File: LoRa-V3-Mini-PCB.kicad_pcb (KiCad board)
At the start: 2 copper layers, 52 x 18 mm, 24 parts, among them Q1 SI2367DS-T1-GE3, SW1 434331045822, SW2 434331045816, U1 114993121, U2 BR24G1MFVT, U3 SHT40, U4 TSL25911

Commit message: move global components into project library
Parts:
- C1, C10, C11, C2, C3, C5: footprint 1GlobalFootprintsLibrary:C_0603_nominal -> 1projectLibrary:C_0603_nominal
- R1, R2, R3, R4: footprint 1GlobalFootprintsLibrary:R_0603_nominal -> 1projectLibrary:R_0603_nominal

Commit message: update 3d models / footprints
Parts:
- U1: footprint 1GlobalFootprintsLibrary:LoRa-E5 -> 1projectLibrary:LoRa-E5
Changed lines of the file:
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@@
 		)
 	)
-	(footprint "1GlobalFootprintsLibrary:LoRa-E5"
+	(footprint "1projectLibrary:LoRa-E5"
 		(layer "F.Cu")
 		(at 150.91 103.5)
@@
 			)
 		)
-		(property "Footprint" "1GlobalFootprintsLibrary:LoRa-E5"
+		(property "Footprint" "1projectLibrary:LoRa-E5"
 			(at 0 13 0)
 			(unlocked yes)
@@
 			(pintype "input+no_connect")
 		)
-		(model "C:/Users/pasca/Documents/Projects/Electronica/myComponents/1global3dmodels/LoRa-E5-HF_3D_File.stp"
+		(model "${KIPRJMOD}/inputs/3dmodels/LoRa-E5-HF_3D_File.stp"
 			(offset
 				(xyz 0 0 2.6)
@@
 	)
 	(zone
-		(net 15)
-		(net_name "SWDIO")
-		(layer "F.Cu")
-		(name "$teardrop_padvia$")
-		(hatch full 0.1)
-		(priority 30010)
-		(attr
-			(teardrop
-				(type padvia)
-			)
-		)
-		(connect_pads yes
-			(clearance 0)
-		)
-		(min_thickness 0.0254)
-		(filled_areas_thickness no)
-		(fill yes
-			(thermal_gap 0.5)
-			(thermal_bridge_width 0.5)
-			(island_removal_mode 1)
-			(island_area_min 10)
-		)
-		(polygon
-			(pts
-				(xy 145.96 102.125) (xy 145.96 102.375) (xy 146.526061 102.573358) (xy 146.661 102.25) (xy 146.526061 101.926642)
-			)
-		)
-	)
-	(zone
 		(net 7)
 		(net_name "I2C2-SDA")
@@
 	)
 	(zone
-		(net 5)
-		(net_name "~{Enable-3.3V-Switched}")
-		(layer "F.Cu")
-		(name "$teardrop_padvia$")
-		(hatch full 0.1)
-		(priority 30012)
-		(attr
-			(teardrop
-				(type padvia)
-			)
-		)
-		(connect_pads yes
-			(clearance 0)
-		)
-		(min_thickness 0.0254)
-		(filled_areas_thickness no)
-		(fill yes
-			(thermal_gap 0.5)
-			(thermal_bridge_width 0.5)
-			(island_removal_mode 1)
-			(island_area_min 10)
-		)
-		(polygon
-			(pts
-				(xy 152.035 108.45) (xy 152.285 108.45) (xy 152.483358 107.883939) (xy 152.16 107.749) (xy 151.836642 107.883939)
-			)
-		)
-	)
-	(zone
 		(net 4)
 		(net_name "+BATT")
@@
 			)
 		)
-	)
-	(zone
-		(net 10)
-		(net_name "Net-(U1-RST)")
-		(layer "F.Cu")
-		(name "$teardrop_padvia$")
-		(hatch full 0.1)
-		(priority 30009)
-		(attr
-			(teardrop
-				(type padvia)
-			)
-		)
-		(connect_pads yes
-			(clearance 0)
-		)
-		(min_thickness 0.0254)
-		(filled_areas_thickness no)
-		(fill yes
-			(thermal_gap 0.5)
-			(thermal_bridge_width 0.5)
-			(island_removal_mode 1)
-			(island_area_min 10)
-		)
-		(polygon
-			(pts
-				(xy 155.86 104.875) (xy 155.86 104.625) (xy 155.293939 104.426642) (xy 155.159 104.75) (xy 155.293939 105.073358)
-			)
-		)

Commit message: using project lib io global
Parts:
- U3: footprint 1GlobalFootprintsLibrary:SHT4X -> 1projectLibrary:SHT4X
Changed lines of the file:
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@@
 		)
 	)
-	(footprint "1GlobalFootprintsLibrary:SHT4X"
+	(footprint "1projectLibrary:SHT4X"
 		(layer "F.Cu")
 		(at 130.41 108.5 180)
@@
 			)
 		)
-		(property "Footprint" "1GlobalFootprintsLibrary:SHT4X"
+		(property "Footprint" "1projectLibrary:SHT4X"
 			(at 0 4 180)
 			(unlocked yes)
@@
 			)
 		)
-		(property "Description" "SHT40"
+		(property "Description" "Digital Relative Humidity Temperature Sensor"
 			(at 0 0 180)
 			(unlocked yes)
@@
 			(pintype "power_in")
 		)
-		(model "C:/Users/pasca/Documents/Projects/Electronica/myComponents/1global3dmodels/SHT40-AD1B-R2.step"
+		(model "${KIPRJMOD}/inputs/3dmodels/SHT40-AD1B-R2.step"
 			(offset
 				(xyz 0 0 0)
@@
 		(attr through_hole)
 		(fp_rect
-			(start 32.004 -8.128)
-			(end -2.54 8.128)
+			(start -2.54 8.128)
+			(end 32.004 -8.128)
 			(stroke
 				(width 0.05)
@@
 			(layer "User.2")
 			(pts
-				(xy 164.914 95.372) (xy 130.37 95.372)
+				(xy 164.914 111.628) (xy 164.914 95.372)
 			)
-			(height 4.572)
-			(gr_text "34,5440 mm"
-				(at 147.642 89.65 0)
+			(height 4.318)
+			(gr_text "16,2560 mm"
+				(at 168.082 103.5 90)
 				(layer "User.2")
 				(effects
@@
 			(layer "User.2")
 			(pts
-				(xy 132.91 103.5) (xy 132.91 110.5866)
+				(xy 132.91 103.5) (xy 162.374 103.5)
 			)
-			(height 4.572)
-			(gr_text "7,0866 mm"
-				(at 127.188 107.0433 90)
+			(height -5.08)
+			(gr_text "29,4640 mm"
+				(at 147.642 97.27 0)
 				(layer "User.2")
 				(effects
@@
 			(layer "User.2")
 			(pts
-				(xy 132.91 103.5) (xy 162.374 103.5)
+				(xy 164.914 95.372) (xy 130.37 95.372)
 			)
-			(height -5.08)
-			(gr_text "29,4640 mm"
-				(at 147.642 97.27 0)
+			(height 4.572)
+			(gr_text "34,5440 mm"
+				(at 147.642 89.65 0)
 				(layer "User.2")
 				(effects
@@
 			(layer "User.2")
 			(pts
-				(xy 164.914 111.628) (xy 164.914 95.372)
+				(xy 132.91 103.5) (xy 132.91 110.5866)
 			)
-			(height 4.318)
-			(gr_text "16,2560 mm"
-				(at 168.082 103.5 90)
+			(height 4.572)
+			(gr_text "7,0866 mm"
+				(at 127.188 107.0433 90)
 				(layer "User.2")
 				(effects
@@
 			(thermal_bridge_angle 0)
 		)
-		(model "C:/Users/pasca/Documents/Projects/Electronica/myComponents/1global3dmodels/Keystone-108.stp"
+		(model "${KIPRJMOD}/inputs/3dmodels/Keystone-108.stp"
 			(offset
 				(xyz 14.75 0 0.4)
@@
 			)
 		)
-	)
-	(zone
-		(net 7)
-		(net_name "I2C2-SDA")
-		(layer "F.Cu")
-		(name "$teardrop_padvia$")
-		(hatch full 0.1)
-		(priority 30007)
-		(attr
-			(teardrop
-				(type padvia)
-			)
-		)
-		(connect_pads yes
-			(clearance 0)
-		)
-		(min_thickness 0.0254)
-		(filled_areas_thickness no)
-		(fill yes
-			(thermal_gap 0.5)
-			(thermal_bridge_width 0.5)
-			(island_removal_mode 1)
-			(island_area_min 10)
-		)
-		(polygon
-			(pts
-				(xy 131.36 108.775) (xy 131.36 109.025) (xy 131.926061 109.223358) (xy 132.061 108.9) (xy 131.926061 108.576642)
-			)
-		)

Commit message: update libraries
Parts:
- ANT1: footprint 1GlobalFootprintsLibrary:XDCR_ANT-868-CHP-T -> 1projectLibrary:XDCR_ANT-868-CHP-T
- F1, F2, F3: footprint Fiducial:Fiducial_0.75mm_Mask1.5mm -> Fiducial:Fiducial_0.5mm_Mask1mm
- SW2: footprint 1GlobalFootprintsLibrary:4341330258X6 -> 1projectLibrary:4341330258X6
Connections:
- SW1 pad 2: SWO -> GND
- SW1 pad 3: GND -> SWO
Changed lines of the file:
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@@
 		)
 	)
-	(footprint "Fiducial:Fiducial_0.75mm_Mask1.5mm"
+	(footprint "Fiducial:Fiducial_0.5mm_Mask1mm"
 		(layer "F.Cu")
 		(at 179.41 111 90)
-		(descr "Circular Fiducial, 0.75mm bare copper, 1.5mm soldermask opening (Level B)")
+		(descr "Circular Fiducial, 0.5mm bare copper, 1mm soldermask opening (Level C)")
 		(tags "fiducial")
 		(property "Reference" "F2"
-			(at 0 -2 -90)
+			(at 0 -1.5 90)
 			(layer "F.SilkS")
 			(hide yes)
@@
 		)
 		(property "Value" "Fiducial"
-			(at 0 2 -90)
+			(at 0 1.5 90)
 			(layer "F.Fab")
 			(effects
@@
 			)
 		)
-		(property "Footprint" "Fiducial:Fiducial_0.75mm_Mask1.5mm"
+		(property "Footprint" "Fiducial:Fiducial_0.5mm_Mask1mm"
 			(at 0 0 90)
 			(unlocked yes)
@@
 		(fp_circle
 			(center 0 0)
-			(end 1 0)
+			(end 0.75 0)
 			(stroke
 				(width 0.05)
@@
 		(fp_circle
 			(center 0 0)
-			(end 0.75 0)
+			(end 0.5 0)
 			(stroke
 				(width 0.1)
@@
 		)
 		(fp_text user "${REFERENCE}"
-			(at 0 0 -90)
+			(at 0 0 90)
 			(layer "F.Fab")
 			(effects
 				(font
-					(size 0.3 0.3)
-					(thickness 0.05)
+					(size 0.2 0.2)
+					(thickness 0.04)
 				)
 			)
@@
 		(pad "" smd circle
 			(at 0 0 90)
-			(size 0.75 0.75)
+			(size 0.5 0.5)
 			(layers "F.Cu" "F.Mask")
-			(solder_mask_margin 0.375)
-			(clearance 0.375)
+			(solder_mask_margin 0.25)
+			(clearance 0.25)
 		)
 	)
-	(footprint "Fiducial:Fiducial_0.75mm_Mask1.5mm"
+	(footprint "Fiducial:Fiducial_0.5mm_Mask1mm"
 		(layer "F.Cu")
 		(at 179.41 96 90)
-		(descr "Circular Fiducial, 0.75mm bare copper, 1.5mm soldermask opening (Level B)")
+		(descr "Circular Fiducial, 0.5mm bare copper, 1mm soldermask opening (Level C)")
 		(tags "fiducial")
 		(property "Reference" "F3"
-			(at 0 -2 -90)
+			(at 0 -1.5 90)
 			(layer "F.SilkS")
 			(hide yes)
@@
 		)
 		(property "Value" "Fiducial"
-			(at 0 2 -90)
+			(at 0 1.5 90)
 			(layer "F.Fab")
 			(effects
@@
 			)
 		)
-		(property "Footprint" "Fiducial:Fiducial_0.75mm_Mask1.5mm"
+		(property "Footprint" "Fiducial:Fiducial_0.5mm_Mask1mm"
 			(at 0 0 90)
 			(unlocked yes)
@@
 		(fp_circle
 			(center 0 0)
-			(end 1 0)
+			(end 0.75 0)
 			(stroke
 				(width 0.05)
@@
 		(fp_circle
 			(center 0 0)
-			(end 0.75 0)
+			(end 0.5 0)
 			(stroke
 				(width 0.1)
@@
 		)
 		(fp_text user "${REFERENCE}"
-			(at 0 0 -90)
+			(at 0 0 90)
 			(layer "F.Fab")
 			(effects
 				(font
-					(size 0.3 0.3)
-					(thickness 0.05)
+					(size 0.2 0.2)
+					(thickness 0.04)
 				)
 			)
@@
 		(pad "" smd circle
 			(at 0 0 90)
-			(size 0.75 0.75)
+			(size 0.5 0.5)
 			(layers "F.Cu" "F.Mask")
-			(solder_mask_margin 0.375)
-			(clearance 0.375)
+			(solder_mask_margin 0.25)
+			(clearance 0.25)
 		)
 	)
@@
 		)
 	)
-	(footprint "1GlobalFootprintsLibrary:XDCR_ANT-868-CHP-T"
+	(footprint "1projectLibrary:XDCR_ANT-868-CHP-T"
 		(layer "F.Cu")
 		(at 171.91 107.25)
@@
 			)
 		)
-		(property "Footprint" "1GlobalFootprintsLibrary:XDCR_ANT-868-CHP-T"
+		(property "Footprint" "1projectLibrary:XDCR_ANT-868-CHP-T"
 			(at 0 5.75 0)
 			(unlocked yes)
@@
 			)
 		)
-		(model "C:/Users/pasca/Documents/Projects/Electronica/myComponents/1global3dmodels/ANT-868-CHP-T.step"
+		(model "${KIPRJMOD}/inputs/3dmodels/ANT-868-CHP-T.step"
 			(offset
 				(xyz 0 0 0)
@@
 		)
 	)
-	(footprint "1GlobalFootprintsLibrary:4341330258X6"
+	(footprint "1projectLibrary:4341330258X6"
 		(layer "F.Cu")
 		(at 137.16 97.5)
 		(property "Reference" "SW2"
-			(at 0 -2.7 0)
+			(at 0.8 -2.7 0)
 			(unlocked yes)
 			(layer "F.SilkS")
@@
 			)
 		)
-		(property "Footprint" "1GlobalFootprintsLibrary:4341330258X6"
+		(property "Footprint" "1projectLibrary:4341330258X6"
 			(at 0.3 4.5 0)
 			(unlocked yes)
@@
 			)
 		)
+		(property "GPN" "NA"
+			(at 0 0 0)
+			(unlocked yes)
+			(layer "F.Fab")
+			(hide yes)
+			(effects
+				(font
+					(size 1 1)
+					(thickness 0.15)
+				)
+			)
+		)
 		(sheetname "Root")
 		(sheetfile "LoRa-V3-Mini-PCB.kicad_sch")
@@
 			)
 		)
-		(pad "1" smd rect
+		(pad "1" smd roundrect
 			(at -2.075 -1.075)
 			(size 1.05 0.65)
 			(layers "F.Cu" "F.Paste" "F.Mask")
+			(roundrect_rratio 0.2)
 			(net 1 "GND")
 			(pinfunction "1")
 			(pintype "passive")
 		)
-		(pad "2" smd rect
+		(pad "2" smd roundrect
 			(at 2.075 -1.075)
 			(size 1.05 0.65)
 			(layers "F.Cu" "F.Paste" "F.Mask")
+			(roundrect_rratio 0.2)
 			(net 1 "GND")
 			(pinfunction "2")
 			(pintype "passive")
 		)
-		(pad "3" smd rect
+		(pad "3" smd roundrect
 			(at -2.075 1.075)
 			(size 1.05 0.65)
 			(layers "F.Cu" "F.Paste" "F.Mask")
+			(roundrect_rratio 0.2)
 			(net 10 "Net-(U1-RST)")
 			(pinfunction "3")
 			(pintype "passive")
 		)
-		(pad "4" smd rect
+		(pad "4" smd roundrect
 			(at 2.075 1.075)
 			(size 1.05 0.65)
 			(layers "F.Cu" "F.Paste" "F.Mask")
+			(roundrect_rratio 0.2)
 			(net 10 "Net-(U1-RST)")
 			(pinfunction "4")
 			(pintype "passive")
 		)
-		(model "C:/Users/pasca/Documents/Projects/Electronica/myComponents/1global3dmodels/4341x30258x6.stp"
+		(model "${KIPRJMOD}/inputs/3dmodels/4341x30258x6.stp"
 			(offset
 				(xyz 0 0 0)
@@
 			)
 		)
-		(property "Datasheet" "https://www.we-online.com/katalog/datasheet/434331045822.pdf"
+		(property "Datasheet" "https://www.we-online.com/components/products/datasheet/434133025816.pdf"
 			(at 0 0 90)
 			(unlocked yes)
@@
 			)
 		)
-		(property "Description" "ApplicationButton"
+		(property "Description" "Application buttonswitch"
 			(at 0 0 90)
 			(unlocked yes)
@@
 			)
 		)
-		(property "manufacturerPartNumber" "434331045822"
+		(property "manufacturerPartNumber" "434133025816"
 			(at 0 0 90)
 			(unlocked yes)
@@
 			(layer "F.Fab")
 		)
-		(fp_text user "SWITCH EDGE"
-			(at -2.75 2.75 -90)
+		(fp_text user "PCB EDGE"
+			(at -3.75 1.75 -90)
 			(layer "Dwgs.User")
 			(hide yes)
 			(effects
 				(font
-					(size 0.2 0.2)
-					(thickness 0.05)
+					(size 0.24 0.24)
+					(thickness 0.06)
 				)
 			)
 		)
-		(fp_text user "PCB EDGE"
-			(at -3.75 1.75 -90)
+		(fp_text user "SWITCH EDGE"
+			(at -2.75 2.75 -90)
 			(layer "Dwgs.User")
 			(hide yes)
 			(effects
 				(font
-					(size 0.24 0.24)
-					(thickness 0.06)
+					(size 0.2 0.2)
+					(thickness 0.05)
 				)
 			)
@@
 			(size 1.2 1)
 			(layers "F.Cu" "F.Paste" "F.Mask")
-			(net 17 "SWO")
+			(net 1 "GND")
 			(pinfunction "2")
 			(pintype "passive")
@@
 			(size 1.2 1)
 			(layers "F.Cu" "F.Paste" "F.Mask")
-			(net 1 "GND")
+			(net 17 "SWO")
 			(pinfunction "3")
 			(pintype "passive")
@@
 		)
 	)
-	(footprint "Fiducial:Fiducial_0.75mm_Mask1.5mm"
+	(footprint "Fiducial:Fiducial_0.5mm_Mask1mm"
 		(layer "F.Cu")
 		(at 130.41 111 90)
-		(descr "Circular Fiducial, 0.75mm bare copper, 1.5mm soldermask opening (Level B)")
+		(descr "Circular Fiducial, 0.5mm bare copper, 1mm soldermask opening (Level C)")
 		(tags "fiducial")
 		(property "Reference" "F1"
-			(at 0 -2 -90)
+			(at 0 -1.5 90)
 			(layer "F.SilkS")
 			(hide yes)
@@
 		)
 		(property "Value" "Fiducial"
-			(at 0 2 -90)
+			(at 0 1.5 90)
 			(layer "F.Fab")
 			(effects
@@
 			)
 		)
-		(property "Footprint" "Fiducial:Fiducial_0.75mm_Mask1.5mm"
+		(property "Footprint" "Fiducial:Fiducial_0.5mm_Mask1mm"
 			(at 0 0 90)
 			(unlocked yes)
@@
 		(fp_circle
 			(center 0 0)
-			(end 1 0)
+			(end 0.75 0)
 			(stroke
 				(width 0.05)
@@
 		(fp_circle
 			(center 0 0)
-			(end 0.75 0)
+			(end 0.5 0)
 			(stroke
 				(width 0.1)
@@
 		)
 		(fp_text user "${REFERENCE}"
-			(at 0 0 -90)
+			(at 0 0 90)
 			(layer "F.Fab")
 			(effects
 				(font
-					(size 0.3 0.3)
-					(thickness 0.05)
+					(size 0.2 0.2)
+					(thickness 0.04)
 				)
 			)
@@
 		(pad "" smd circle
 			(at 0 0 90)
-			(size 0.75 0.75)
+			(size 0.5 0.5)
 			(layers "F.Cu" "F.Mask")
-			(solder_mask_margin 0.375)
-			(clearance 0.375)
+			(solder_mask_margin 0.25)
+			(clearance 0.25)
 		)
 	)
@@
 	)
 	(zone
-		(net 17)
-		(net_name "SWO")
-		(layer "F.Cu")
-		(name "$teardrop_padvia$")
-		(hatch full 0.1)
-		(priority 30022)
-		(attr
-			(teardrop
-				(type padvia)
-			)
-		)
-		(connect_pads yes
-			(clearance 0)
-		)
-		(min_thickness 0.0254)
-		(filled_areas_thickness no)
-		(fill yes
-			(thermal_gap 0.5)
-			(thermal_bridge_width 0.5)
-			(island_removal_mode 1)
-			(island_area_min 10)
-		)
-		(polygon
-			(pts
-				(xy 131.86 96.7) (xy 131.66 96.7) (xy 131.436642 97.266061) (xy 131.76 97.401) (xy 132.083358 97.266061)
-			)
-		)
-	)
-	(zone

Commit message: update application switch
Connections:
- SW1 pad 2: GND -> SWO
- SW1 pad 3: SWO -> GND

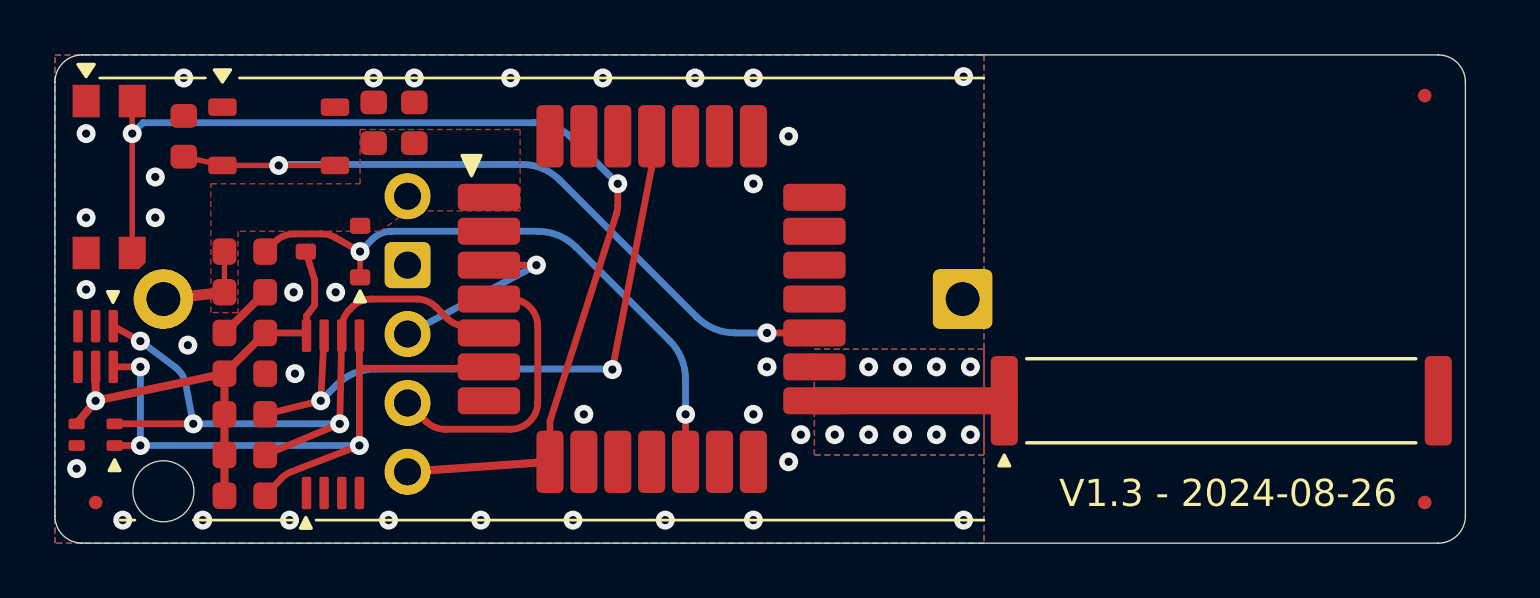
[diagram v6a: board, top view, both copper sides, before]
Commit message: upgraded debug connector with UART1TX
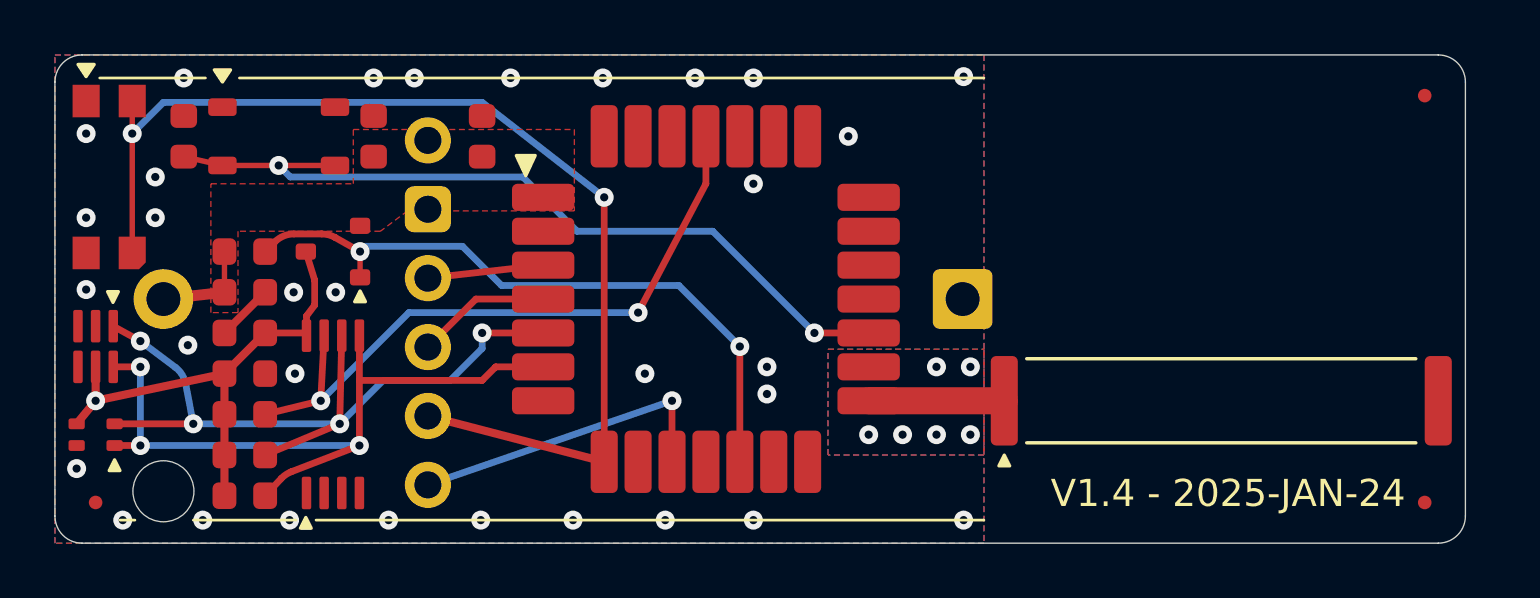
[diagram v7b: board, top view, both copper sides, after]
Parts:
- CONN5: footprint 1projectLibrary:PinHeader_1x05_P2.54mm_Vertical -> 1projectLibrary:DebugConnector_1x06_P2.54mm
- Q1: footprint 1GlobalFootprintsLibrary:SI2367DS-SOT-23 -> 1projectLibrary:SI2367DS-SOT-23
- moved C3 2.55 mm to (144.7, 97.5)
- moved U1 2.00 mm to (152.9, 103.5)
- moved CONN5 1.90 mm to (142.7, 104.0), turned to 0 degrees
- moved C11 0.50 mm to (140.7, 97.5)
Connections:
- U1 pad 10: unconnected-(U1-PB6-Pad10) -> UART1-TX
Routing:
- net UART1-TX: track 0.00 -> 11.8 mm, vias 0 -> 1
- net SWCLK: track 10.8 -> 4.98 mm
- net I2C2-SCL: track 26.2 -> 29.0 mm, vias 3 -> 4
- net SWDIO: track 7.14 -> 4.53 mm, vias 1 -> 0
- net I2C2-SDA: track 25.8 -> 28.0 mm
- net Net-(U1-RST): track 27.8 -> 29.9 mm
- net ~{Enable-3.3V-Switched}: track 22.7 -> 24.7 mm
- net RF: track 7.00 -> 5.00 mm
- net SWO: track 40.4 -> 41.1 mm
- net GND: track 2.33 -> 2.53 mm, vias 43 -> 38
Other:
- board text added: "V1.4 - 2025-JAN-24"
- board text removed: "V1.3 - 2024-08-26"

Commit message: finishing touch to layout
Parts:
- G***: footprint 1GlobalFootprintsLibrary:cc-logo -> 1projectLibrary:cc-logo
- U2: footprint 1GlobalFootprintsLibrary:BR24G1M-TSSOP-B8 -> 1projectLibrary:BR24G1M-TSSOP-B8
- U4: footprint 1GlobalFootprintsLibrary:TSL2591 -> 1projectLibrary:TSL2591-SON
- moved CONN5 0.50 mm to (142.7, 103.5)
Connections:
- U2 pad 1: unconnected-(U2-A0-Pad1) -> GND
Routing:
- net 3.3V-Switched: track 18.7 -> 11.5 mm, vias 1 -> 0
- net I2C2-SDA: track 28.0 -> 32.9 mm, vias 3 -> 4
- net ~{WRITE-PROTECT}: track 24.7 -> 26.7 mm
- net SWO: track 41.1 -> 42.5 mm
- net I2C2-SCL: track 29.0 -> 30.2 mm
- net UART1-TX: track 11.8 -> 10.8 mm, vias 1 -> 0
- net ~{Enable-3.3V-Switched}: track 24.7 -> 25.7 mm
- net Net-(U1-RST): track 29.9 -> 29.4 mm
- added copper zone on F.Cu, net 3.3V-Switched
